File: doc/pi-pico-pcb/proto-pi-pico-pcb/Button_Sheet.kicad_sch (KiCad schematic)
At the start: 2 parts

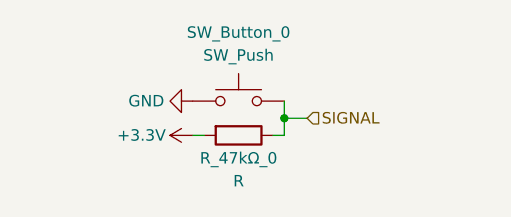
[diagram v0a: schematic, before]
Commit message: added flash memory
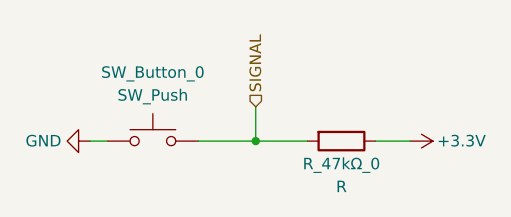
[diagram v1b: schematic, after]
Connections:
- net +3.3V: now also R_47kΩ_0.1; no longer R_47kΩ_0.2
- net SIGNAL: now also R_47kΩ_0.2; no longer R_47kΩ_0.1
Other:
- company: (none) -> PROTO
- moved on the sheet: R_47kΩ_0, SW_Button_0
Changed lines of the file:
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@@
 (kicad_sch (version 20211123) (generator eeschema)
   (paper "A4")
-  (junction (at 153.035 100.965) (diameter 0) (color 0 0 0 0)
+  (title_block
+    (date "2025-09-09")
+    (rev "1")
+    (company "PROTO")
+    (comment 1 "Author: Carston Wiebe")
   )
-  (wire (pts (xy 151.765 102.87) (xy 153.035 102.87))
+  (junction (at 149.86 103.505) (diameter 0) (color 0 0 0 0)
+  )
+  (wire (pts (xy 149.86 99.695) (xy 149.86 103.505))
     (stroke (width 0) (type default) (color 0 0 0 0))
   )
-  (wire (pts (xy 153.035 100.965) (xy 155.575 100.965))
+  (wire (pts (xy 143.51 103.505) (xy 149.86 103.505))
     (stroke (width 0) (type default) (color 0 0 0 0))
   )
-  (wire (pts (xy 153.035 100.965) (xy 153.035 99.06))
+  (wire (pts (xy 167.005 103.505) (xy 163.195 103.505))
     (stroke (width 0) (type default) (color 0 0 0 0))
   )
-  (wire (pts (xy 142.875 102.87) (xy 144.145 102.87))
+  (wire (pts (xy 149.86 103.505) (xy 155.575 103.505))
     (stroke (width 0) (type default) (color 0 0 0 0))
   )
-  (wire (pts (xy 153.035 102.87) (xy 153.035 100.965))
+  (wire (pts (xy 133.35 103.505) (xy 131.445 103.505))
     (stroke (width 0) (type default) (color 0 0 0 0))
   )
-  (hierarchical_label "SIGNAL" (shape input) (at 155.575 100.965 0)
+  (hierarchical_label "SIGNAL" (shape input) (at 149.86 99.695 90)
     (effects (font (size 1.27 1.27)) (justify left))
   )
-  (symbol (lib_id "Device:R") (at 147.955 102.87 270) (unit 1)
+  (symbol (lib_id "Device:R") (at 159.385 103.505 270) (unit 1)
     (in_bom yes) (on_board yes)
-    (property "Reference" "R_47kΩ_0" (id 0) (at 147.955 105.41 90))
-    (property "Value" "R" (id 1) (at 147.955 107.95 90))
-    (property "Footprint" "Resistor_SMD:R_0201_0603Metric" (id 2) (at 147.955 101.092 90)
+    (property "Reference" "R_47kΩ_0" (id 0) (at 159.385 106.045 90))
+    (property "Value" "R" (id 1) (at 159.385 108.585 90))
+    (property "Footprint" "Resistor_SMD:R_0201_0603Metric" (id 2) (at 159.385 101.727 90)
       (effects (font (size 1.27 1.27)) hide)
     )
-    (property "Datasheet" "~" (id 3) (at 147.955 102.87 0)
+    (property "Datasheet" "~" (id 3) (at 159.385 103.505 0)
       (effects (font (size 1.27 1.27)) hide)
     )
@@
     (pin "2")
   )
-  (symbol (lib_id "power:GND") (at 142.875 99.06 270) (unit 1)
+  (symbol (lib_id "power:GND") (at 131.445 103.505 270) (unit 1)
     (in_bom yes) (on_board yes)
-    (property "Reference" "#PWR0108" (id 0) (at 136.525 99.06 0)
+    (property "Reference" "#PWR0108" (id 0) (at 125.095 103.505 0)
       (effects (font (size 1.27 1.27)) hide)
     )
-    (property "Value" "GND" (id 1) (at 139.7 99.06 90)
+    (property "Value" "GND" (id 1) (at 128.27 103.505 90)
       (effects (font (size 1.27 1.27)) (justify right))
     )
-    (property "Footprint" "" (id 2) (at 142.875 99.06 0)
+    (property "Footprint" "" (id 2) (at 131.445 103.505 0)
       (effects (font (size 1.27 1.27)) hide)
     )
-    (property "Datasheet" "" (id 3) (at 142.875 99.06 0)
+    (property "Datasheet" "" (id 3) (at 131.445 103.505 0)
       (effects (font (size 1.27 1.27)) hide)
     )
     (pin "1")
   )
-  (symbol (lib_id "Switch:SW_Push") (at 147.955 99.06 0) (unit 1)
+  (symbol (lib_id "Switch:SW_Push") (at 138.43 103.505 0) (unit 1)
     (in_bom yes) (on_board yes)
-    (property "Reference" "SW_Button_0" (id 0) (at 147.955 91.44 0))
-    (property "Value" "SW_Push" (id 1) (at 147.955 93.98 0))
-    (property "Footprint" "Button_Switch_SMD:Panasonic_EVQPUJ_EVQPUA" (id 2) (at 147.955 93.98 0)
+    (property "Reference" "SW_Button_0" (id 0) (at 138.43 95.885 0))
+    (property "Value" "SW_Push" (id 1) (at 138.43 98.425 0))
+    (property "Footprint" "Button_Switch_SMD:Panasonic_EVQPUJ_EVQPUA" (id 2) (at 138.43 98.425 0)
       (effects (font (size 1.27 1.27)) hide)
     )
-    (property "Datasheet" "~" (id 3) (at 147.955 93.98 0)
+    (property "Datasheet" "~" (id 3) (at 138.43 98.425 0)
       (effects (font (size 1.27 1.27)) hide)
     )
@@
     (pin "2")
   )
-  (symbol (lib_id "power:+3.3V") (at 142.875 102.87 90) (unit 1)
+  (symbol (lib_id "power:+3.3V") (at 167.005 103.505 270) (unit 1)
     (in_bom yes) (on_board yes)
-    (property "Reference" "#PWR0106" (id 0) (at 146.685 102.87 0)
+    (property "Reference" "#PWR0106" (id 0) (at 163.195 103.505 0)
       (effects (font (size 1.27 1.27)) hide)
     )
-    (property "Value" "+3.3V" (id 1) (at 137.16 102.87 90))
-    (property "Footprint" "" (id 2) (at 142.875 102.87 0)
+    (property "Value" "+3.3V" (id 1) (at 172.72 103.505 90))
+    (property "Footprint" "" (id 2) (at 167.005 103.505 0)
       (effects (font (size 1.27 1.27)) hide)
     )
-    (property "Datasheet" "" (id 3) (at 142.875 102.87 0)
+    (property "Datasheet" "" (id 3) (at 167.005 103.505 0)
       (effects (font (size 1.27 1.27)) hide)
     )
